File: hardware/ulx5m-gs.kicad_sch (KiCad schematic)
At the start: 4 parts

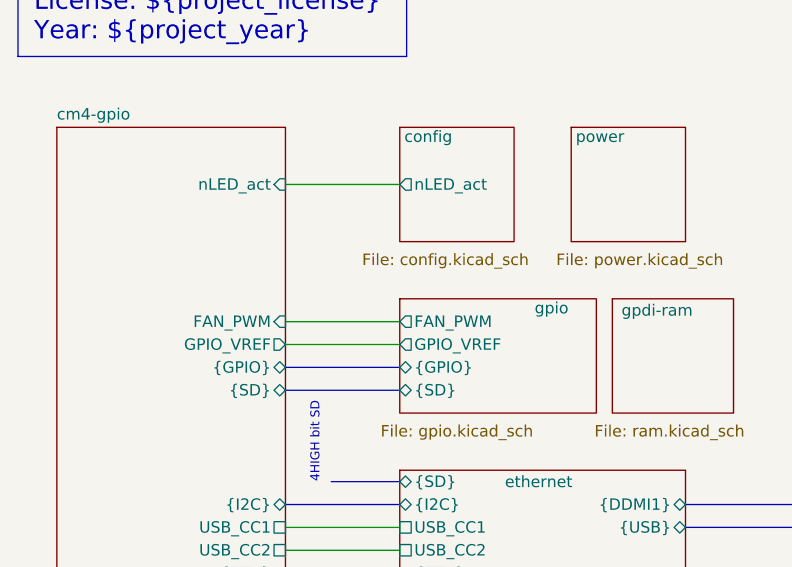
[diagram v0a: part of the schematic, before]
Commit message: Adding JTAG over GPIO
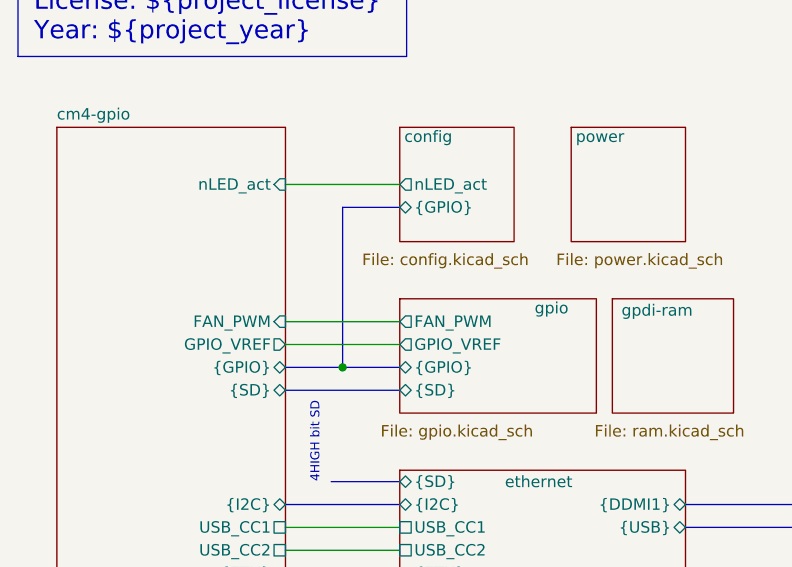
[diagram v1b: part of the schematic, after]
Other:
- sheet config ports: added {GPIO}; removed none
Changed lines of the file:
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@@
 		)
+	)
+	(junction
+		(at 52.07 66.04)
+		(diameter 0)
+		(color 0 0 0 0)
 	)
 	(no_connect
@@
 	(bus
 		(pts
+			(xy 52.07 48.26) (xy 58.42 48.26)
+		)
+		(stroke
+			(width 0)
+			(type default)
+			(color 255 0 255 1)
+		)
+	)
+	(bus
+		(pts
 			(xy 90.17 106.68) (xy 102.87 106.68)
 		)
@@
 	(bus
 		(pts
+			(xy 52.07 66.04) (xy 52.07 48.26)
+		)
+		(stroke
+			(width 0)
+			(type default)
+			(color 255 0 255 1)
+		)
+	)
+	(bus
+		(pts
 			(xy 90.17 101.6) (xy 102.87 101.6)
 		)
@@
 	(bus
 		(pts
-			(xy 45.72 66.04) (xy 58.42 66.04)
+			(xy 45.72 66.04) (xy 52.07 66.04)
+		)
+		(stroke
+			(width 0)
+			(type default)
+			(color 255 0 255 1)
+		)
+	)
+	(bus
+		(pts
+			(xy 52.07 66.04) (xy 58.42 66.04)
 		)
 		(stroke
@@
 			(effects
 				(font
+					(size 1.27 1.27)
+				)
+				(justify left)
+			)
+		)
+		(pin "{GPIO}" bidirectional
+			(at 58.42 48.26 180)
+			(effects
+				(font

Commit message: CleanUP
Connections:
- no-connect marks 8 -> 7
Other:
- sheet cm4-gpio ports: added none; removed PWR_BTN
- sheet lvds ports: added none; removed PWR_BTN
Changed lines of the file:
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@@
-	)
-	(no_connect
-		(at 45.72 107.95)
 	)
 	(no_connect
@@
 			(width 0)
 			(type default)
-		)
-	)
-	(wire
-		(pts
-			(xy 45.72 105.41) (xy 58.42 105.41)
-		)
-		(stroke
-			(width 0)
-			(type default)
-			(color 255 0 255 1)
 		)
 	)
@@
 			)
 		)
-		(pin "PWR_BTN" output
-			(at 45.72 105.41 0)
-			(effects
-				(font
-					(size 1.27 1.27)
-				)
-				(justify right)
-			)
-		)
 		(pin "USB_CC1" passive
 			(at 45.72 83.82 0)
@@
 			)
 		)
-		(pin "PWR_BTN" input
-			(at 58.42 105.41 180)
-			(effects
-				(font
-					(size 1.27 1.27)
-				)
-				(justify left)
-			)
-		)
